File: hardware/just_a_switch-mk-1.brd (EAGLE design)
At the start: 100 x 80 mm, 9 parts, among them Q1 2N7000

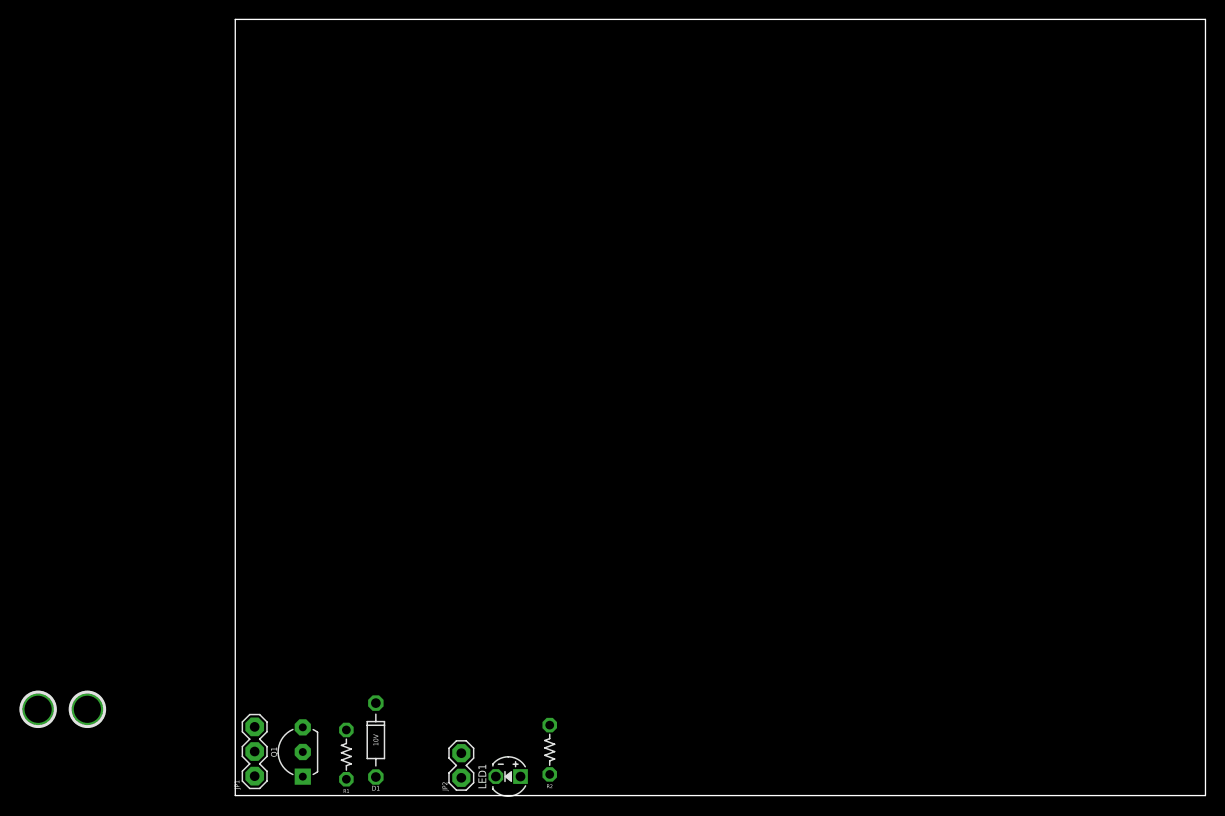
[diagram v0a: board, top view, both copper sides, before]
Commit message: Stupid simple N-MOSFET breakout with LED for debugging
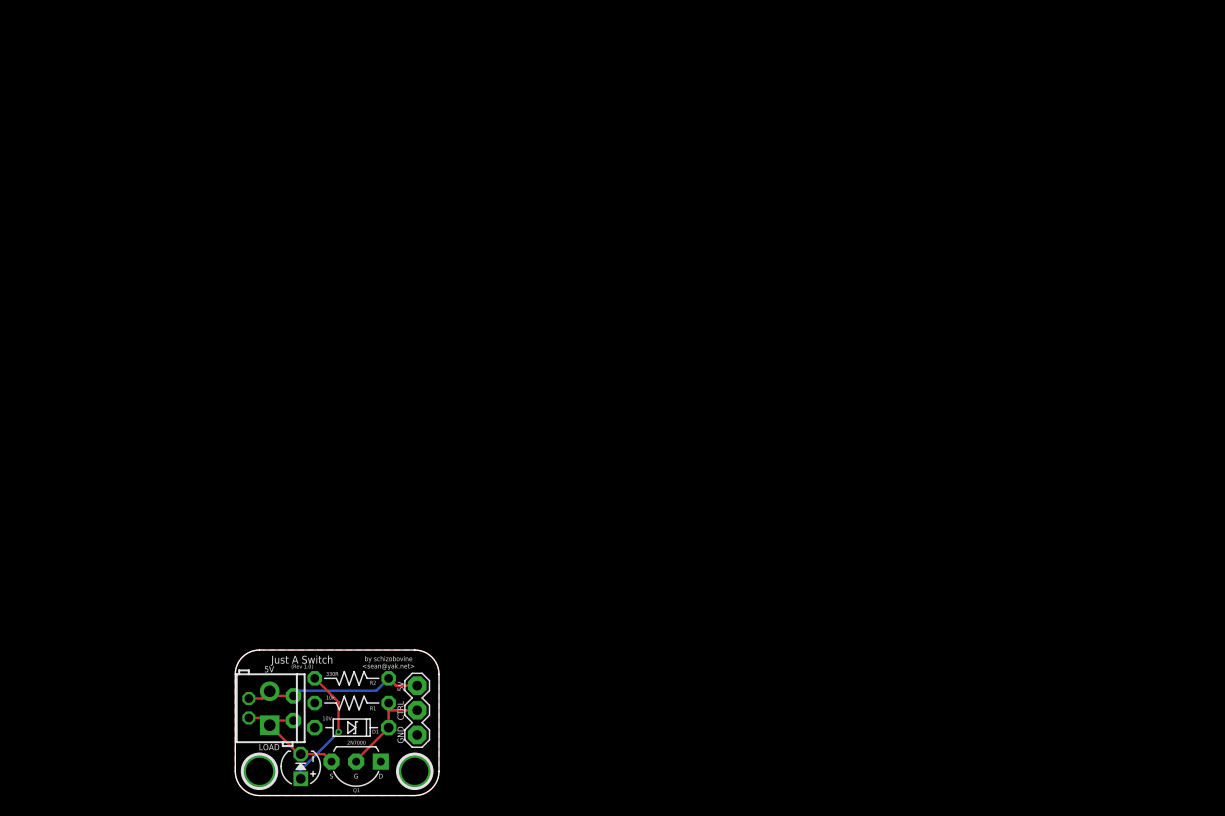
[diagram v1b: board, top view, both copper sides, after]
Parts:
- removed JP1: M03PTH, A_butts:1X03
- removed JP2: M02PTH, A_butts:1X02
- added CTRL: M03PTH, A_butts:1X03
- added LOAD0: M02PTH-2MM, A_butts:1X02-2MM-PTH
- added LOAD1: M021X02_NO_SILK, A_butts:1X02_NO_SILK
- added LOAD2: M023.5MM, A_butts:SCREWTERMINAL-3.5MM-2
- added U$1: (no value), A_butts:CC-BY-SA-4.0-NO-URL
- D1: device A_butts:DIODE-7.68MM -> A_butts:DIODE-7.62MM
- R1, R2: device A_butts:RESISTOR-AXIAL-PTH-5.08MM -> A_butts:RESISTOR-AXIAL-PTH-7.62MM
- moved H2 39.3 mm to (18.5, 2.50), turned to 180 degrees
- moved R2 21.7 mm to (12.0, 12.1), turned to 0 degrees
- moved LED1 21.4 mm to (6.75, 3.00), turned to 90 degrees
- moved H1 18.9 mm to (2.50, 2.50), turned to 180 degrees
- moved Q1 5.59 mm to (12.5, 3.50), turned to 180 degrees
- moved R1 5.35 mm to (12.0, 9.54), turned to 0 degrees
- moved D1 2.80 mm to (12.0, 7.00), turned to 0 degrees
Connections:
- removed net N$3: JP2.1, LED1.K, Q1.3
- new net LOAD: LED1.K, LOAD0.P$1, LOAD1.1, LOAD2.1, Q1.3
- net GND: now also CTRL.1; no longer JP1.1
- net N$1: now also CTRL.2; no longer JP1.2
- net VCC: now also CTRL.3, LOAD0.P$2, LOAD1.2, LOAD2.2; no longer JP1.3, JP2.2
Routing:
- net VCC: track 0.00 -> 18.9 mm
- net LOAD: track 0.00 -> 13.0 mm
- net N$2: track 0.00 -> 13.0 mm, vias 0 -> 1
- net N$1: track 0.00 -> 10.4 mm
- added copper zone on layer 1, net GND
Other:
- board size 100 x 80 mm -> 21 x 15 mm
- board text added: "(Rev 1.0)"
- board text added: "5V"
- board text added: "CTRL"
- board text added: "D"
- board text added: "D1=10V Zener (Q1 protector)"
- board text added: "G"
- board text added: "GND"
- board text added: "Just A Switch"
- board text added: "LOAD"
- board text added: "Q1"
- board text added: "R1=pulldown/Q1 NO"
- board text added: "R2=330R (LED)"
- board text added: "S"
- board text added: "by schizobovine <sean@yak.net>"
